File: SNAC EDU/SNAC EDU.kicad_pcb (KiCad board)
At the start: 2 copper layers, 60 x 50 mm, 52 parts, among them J1 JST-PH, J2 JST-PH, J3 USB3_A, J4 Conn_01x08_Pin, J5 Conn_01x08_Pin, J6 Conn_01x02_Pin, J7 Conn_01x05_Pin, Q1 BSS138, Q2 BSS138, Q3 BSS138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

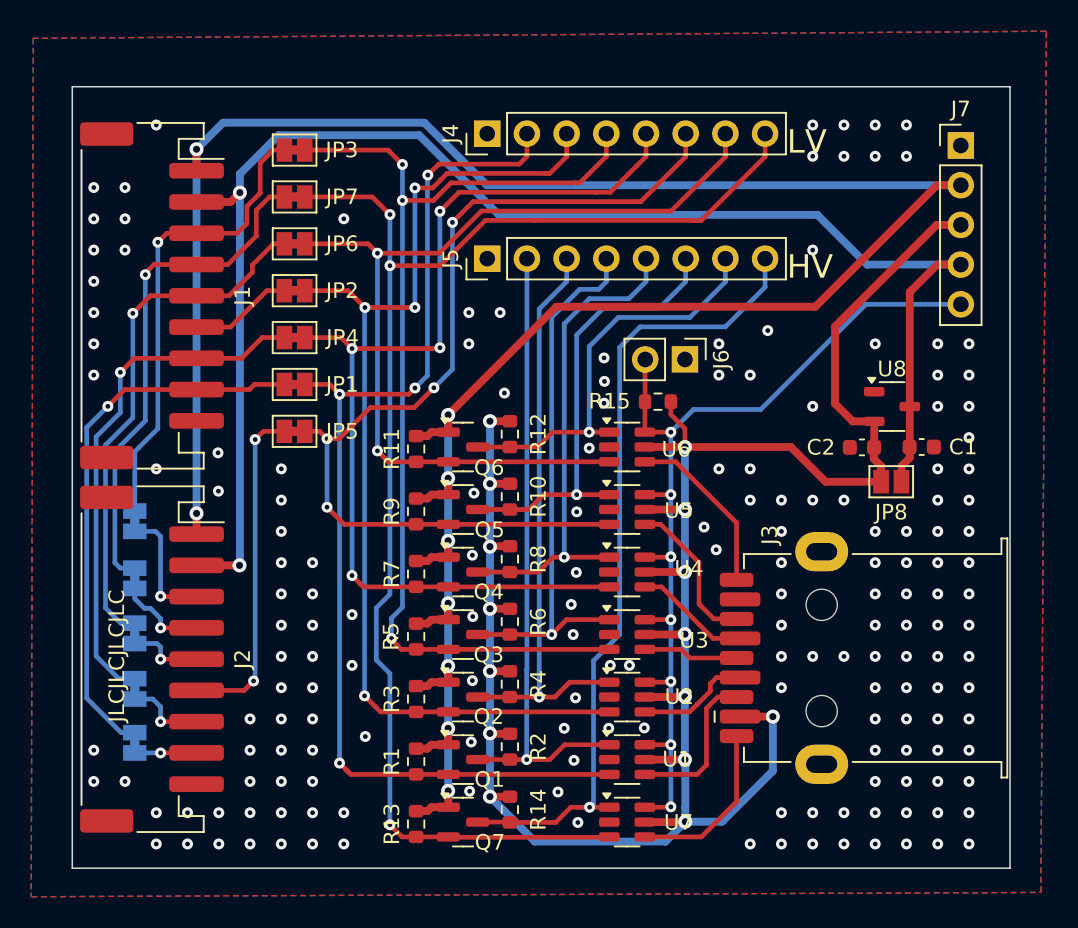
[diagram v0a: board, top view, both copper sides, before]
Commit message: added connector labels and jumpers for P2 data lines
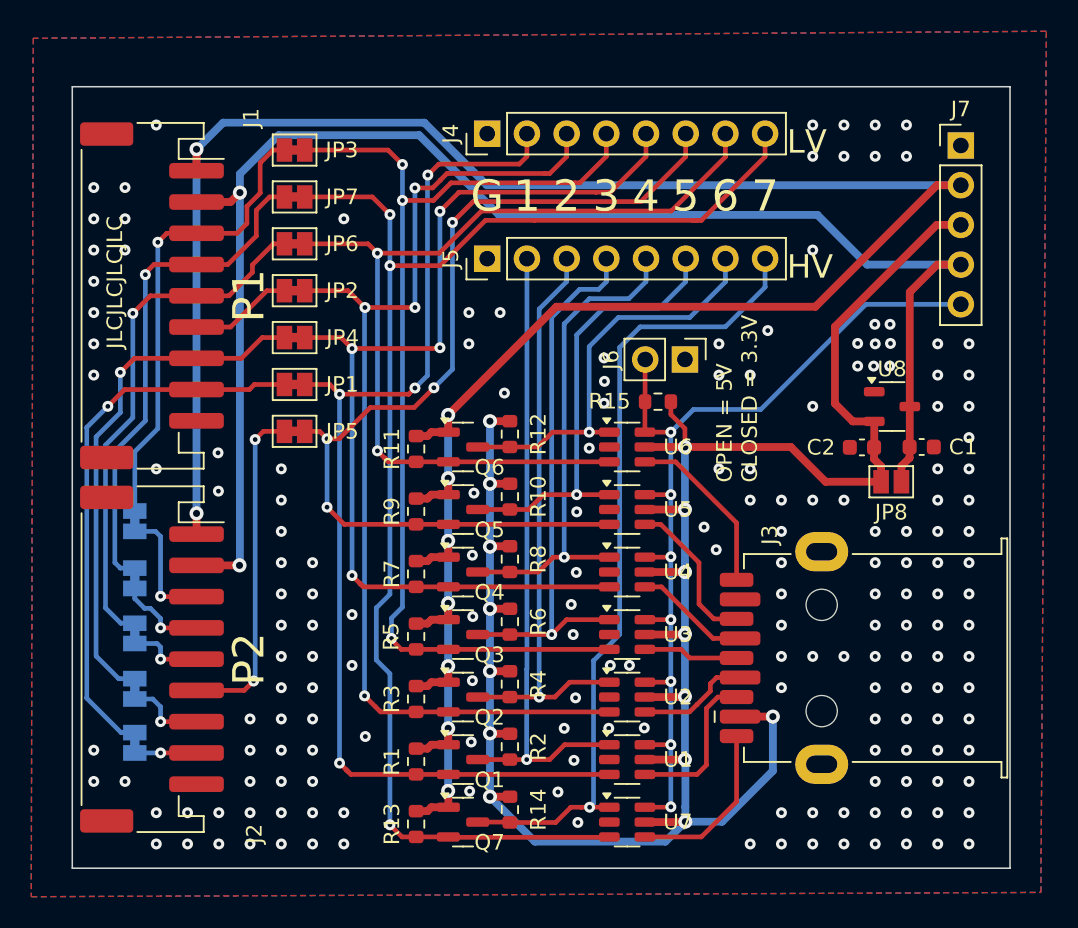
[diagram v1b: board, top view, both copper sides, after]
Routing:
- net GND: vias 177 -> 184
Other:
- board text added: "1"
- board text added: "2"
- board text added: "3"
- board text added: "4"
- board text added: "5"
- board text added: "6"
- board text added: "7"
- board text added: "G"
- board text added: "OPEN = 5V CLOSED = 3.3V"
- board text added: "P1"
- board text added: "P2"
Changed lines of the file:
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@@
 		(tags "SOT TO_SOT_SMD")
 		(property "Reference" "Q2"
-			(at 1.65 1.25 0)
+			(at 1.7 1.3 0)
 			(layer "F.SilkS")
 			(effects
@@
 		(tags "SOT TO_SOT_SMD")
 		(property "Reference" "Q3"
-			(at 1.65 1.3 0)
+			(at 1.7 1.3 0)
 			(layer "F.SilkS")
 			(effects
@@
 		(tags "TSOT TO_SOT_SMD")
 		(property "Reference" "U5"
-			(at 3.3125 0.075 0)
+			(at 3.25 0 0)
 			(layer "F.SilkS")
 			(effects
@@
 		(tags "SOT TO_SOT_SMD")
 		(property "Reference" "Q1"
-			(at 1.7 1.275 0)
+			(at 1.7 1.3 0)
 			(layer "F.SilkS")
 			(effects
@@
 		(tags "TSOT TO_SOT_SMD")
 		(property "Reference" "U7"
-			(at 3.2875 0.025 0)
+			(at 3.25 0 0)
 			(layer "F.SilkS")
 			(effects
@@
 		(tags "Through hole pin header THT 1x02 2.54mm single row")
 		(property "Reference" "J6"
-			(at 0 -2.33 90)
+			(at 0.025 4.725 90)
 			(layer "F.SilkS")
 			(effects
@@
 		(tags "SOT TO_SOT_SMD")
 		(property "Reference" "Q7"
-			(at 1.725 1.3 0)
+			(at 1.7 1.3 0)
 			(layer "F.SilkS")
 			(effects
@@
 		(tags "SOT TO_SOT_SMD")
 		(property "Reference" "Q4"
-			(at 1.65 1.275 0)
+			(at 1.7 1.3 0)
 			(layer "F.SilkS")
 			(effects
@@
 		(tags "SOT TO_SOT_SMD")
 		(property "Reference" "Q6"
-			(at 1.675 1.325 0)
+			(at 1.7 1.3 0)
 			(layer "F.SilkS")
 			(effects
@@
 		(tags "TSOT TO_SOT_SMD")
 		(property "Reference" "U4"
-			(at 3.9625 -0.225 0)
+			(at 3.25 0 0)
 			(layer "F.SilkS")
 			(effects
@@
 		(tags "TSOT TO_SOT_SMD")
 		(property "Reference" "U1"
-			(at 3.1875 -0.025 0)
+			(at 3.25 0 0)
 			(layer "F.SilkS")
 			(effects
@@
 		(tags "TSOT TO_SOT_SMD")
 		(property "Reference" "U2"
-			(at 3.3375 -0.025 0)
+			(at 3.25 0 0)
 			(layer "F.SilkS")
 			(effects
@@
 		(tags "TSOT TO_SOT_SMD")
 		(property "Reference" "U3"
-			(at 4.2875 0.375 0)
+			(at 3.25 0 0)
 			(layer "F.SilkS")
 			(effects
@@
 		(tags "connector JST PH horizontal")
 		(property "Reference" "J2"
-			(at 0 -5.8 90)
+			(at 11.175 -6.55 90)
 			(layer "F.SilkS")
 			(effects
@@
 		(tags "connector JST PH horizontal")
 		(property "Reference" "J1"
-			(at 0 -5.8 -90)
+			(at -11.375 -6.35 -90)
 			(layer "F.SilkS")
 			(effects
@@
 		(tags "TSOT TO_SOT_SMD")
 		(property "Reference" "U6"
-			(at 3.1375 0.15 0)
+			(at 3.25 0 0)
 			(layer "F.SilkS")
 			(effects
@@
 	)
 	(gr_text "JLCJLCJLCJLC"
-		(at 127.85 136.425 90)
+		(at 127.725 112.525 90)
 		(layer "F.SilkS")
 		(effects
@@
 		)
 	)
+	(gr_text "5"
+		(at 164.25 107 0)
+		(layer "F.SilkS")
+		(effects
+			(font
+				(size 2 2)
+				(thickness 0.3)
+			)
+		)
+	)
+	(gr_text "P2"
+		(at 136.3 136.625 90)
+		(layer "F.SilkS")
+		(effects
+			(font
+				(size 2 2)
+				(thickness 0.3)
+			)
+		)
+	)
+	(gr_text "3"
+		(at 159.17 107 0)
+		(layer "F.SilkS")
+		(effects
+			(font
+				(size 2 2)
+				(thickness 0.3)
+			)
+		)
+	)
+	(gr_text "G"
+		(at 151.55 107 0)
+		(layer "F.SilkS")
+		(effects
+			(font
+				(size 2 2)
+				(thickness 0.3)
+			)
+		)
+	)
+	(gr_text "7"
+		(at 169.33 107 0)
+		(layer "F.SilkS")
+		(effects
+			(font
+				(size 2 2)
+				(thickness 0.3)
+			)
+		)
+	)
 	(gr_text "LV"
 		(at 170.725 104.4 0)
@@
 		)
 	)
+	(gr_text "1"
+		(at 154.09 107 0)
+		(layer "F.SilkS")
+		(effects
+			(font
+				(size 2 2)
+				(thickness 0.3)
+			)
+		)
+	)
+	(gr_text "6"
+		(at 166.79 107 0)
+		(layer "F.SilkS")
+		(effects
+			(font
+				(size 2 2)
+				(thickness 0.3)
+			)
+		)
+	)
+	(gr_text "P1"
+		(at 136.3 113.375 90)
+		(layer "F.SilkS")
+		(effects
+			(font
+				(size 2 2)
+				(thickness 0.3)
+			)
+		)
+	)
+	(gr_text "4"
+		(at 161.71 107 0)
+		(layer "F.SilkS")
+		(effects
+			(font
+				(size 2 2)
+				(thickness 0.3)
+			)
+		)
+	)
+	(gr_text "OPEN = 5V\nCLOSED = 3.3V"
+		(at 168.925 125.325 90)
+		(layer "F.SilkS")
+		(effects
+			(font
+				(size 1 1)
+				(thickness 0.15)
+			)
+			(justify left bottom)
+		)
+	)
+	(gr_text "2"
+		(at 156.63 107 0)
+		(layer "F.SilkS")
+		(effects
+			(font
+				(size 2 2)
+				(thickness 0.3)
+			)
+		)
+	)
 	(gr_text "HV\n"
 		(at 170.725 112.4 0)
@@
 	)
 	(via
+		(at 176.35 115.2)
+		(size 0.7)
+		(drill 0.3)
+		(layers "F.Cu" "B.Cu")
+		(free yes)
+		(net 1)
+	)
+	(via
 		(at 157.275 127.2)
 		(size 0.7)
@@
 	)
 	(via
+		(at 175.25 116.425)
+		(size 0.7)
+		(drill 0.3)
+		(layers "F.Cu" "B.Cu")
+		(free yes)
+		(net 1)
+	)
+	(via
 		(at 161.6 141.025)
 		(size 0.7)
@@
 	)
 	(via
+		(at 177.325 115.2)
+		(size 0.7)
+		(drill 0.3)
+		(layers "F.Cu" "B.Cu")
+		(free yes)
+		(net 1)
+	)
+	(via
 		(at 138.375 134.45)
 		(size 0.7)
@@
 	)
 	(via
+		(at 175.25 117.875)
+		(size 0.7)
+		(drill 0.3)
+		(layers "F.Cu" "B.Cu")
+		(free yes)
+		(net 1)
+	)
+	(via
 		(at 159.05 118.85)
 		(size 0.7)
@@
 	)
 	(via
+		(at 177.3 117.875)
+		(size 0.7)
+		(drill 0.3)
+		(layers "F.Cu" "B.Cu")
+		(free yes)
+		(net 1)
+	)
+	(via
 		(at 182.375 140.45)
 		(size 0.7)
@@
 		(size 0.7)
 		(drill 0.3)
+		(layers "F.Cu" "B.Cu")
+		(free yes)
+		(net 1)
+	)
+	(via
+		(at 177.35 116.425)
+		(size 0.7)
+		(drill 0.3)
+		(layers "F.Cu" "B.Cu")
+		(free yes)
+		(net 1)
+	)
+	(via
+		(at 176.275 117.875)
+		(size 0.7)
+		(drill 0.3)
